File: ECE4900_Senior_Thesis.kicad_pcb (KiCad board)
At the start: 2 copper layers, 9 parts, among them Q1 CSD18540Q5B, Q2 CSD18540Q5B, Q4 CSD18540Q5B, U1 UCC27301ADR, U3 STM32G474CBT6TR, U5 INA240A2DR, U6 INA240A2DR, U7 LM74700QDBVRQ1

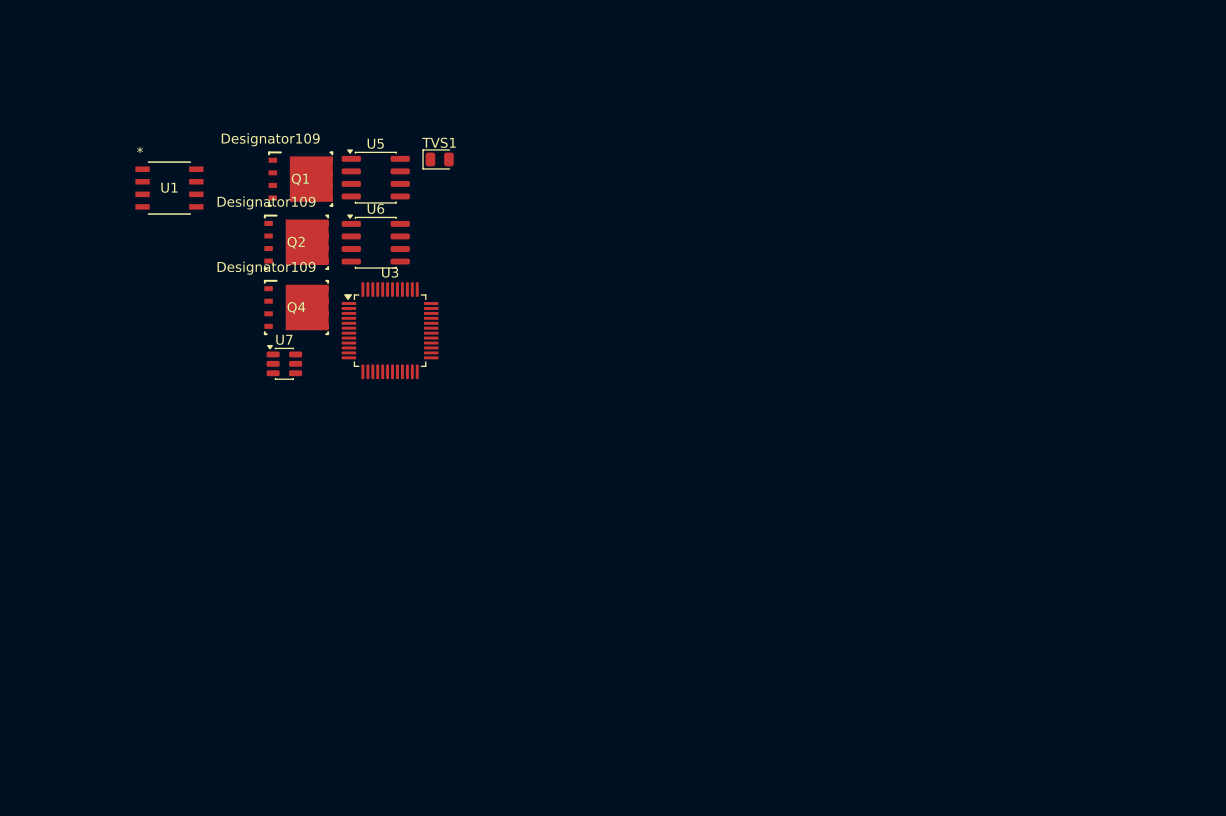
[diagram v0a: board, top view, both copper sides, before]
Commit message: Preliminary Layout Finished
Further pre-fab inspection is neccessary
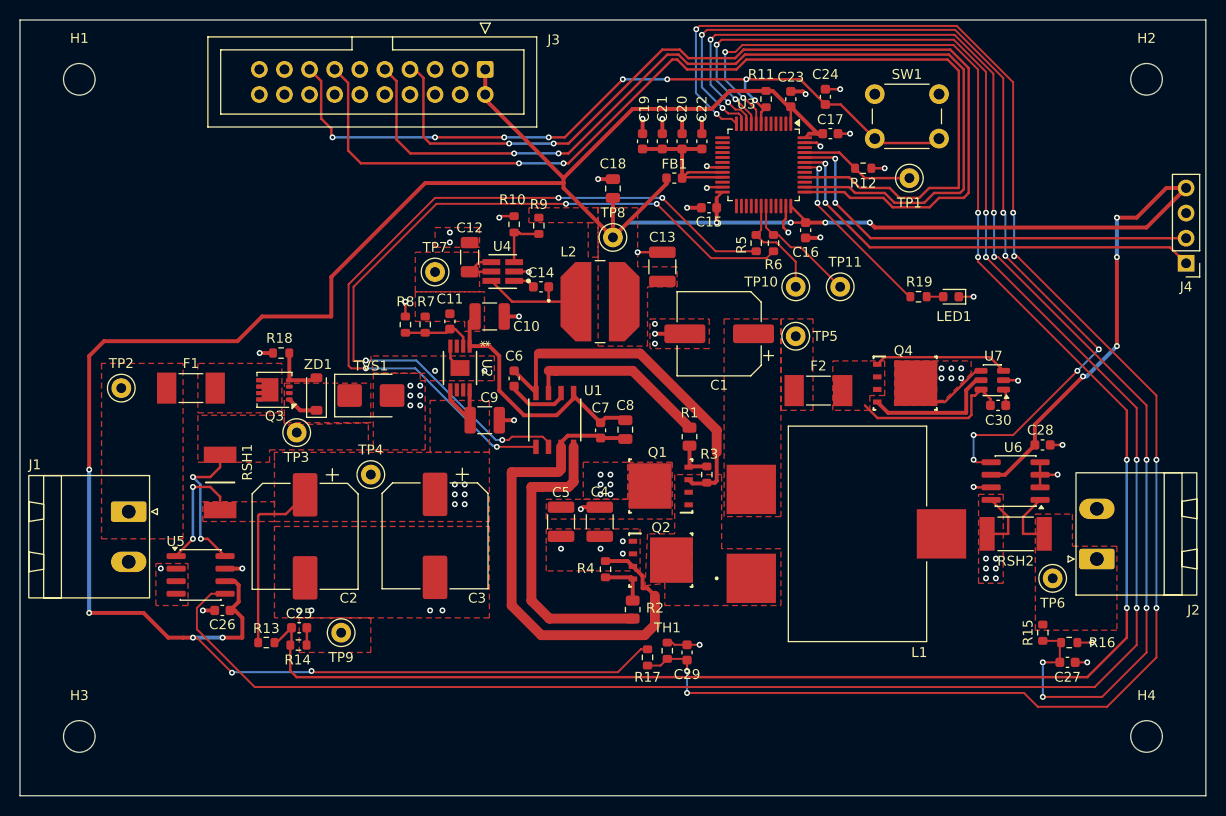
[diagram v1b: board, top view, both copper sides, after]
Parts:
- added C1: 100uF, Capacitor_SMD:CP_Elec_8x6.9, F.Cu at (120.8, 81.8)
- added C10: 10uF, Capacitor_SMD:C_1210_3225Metric, F.Cu at (97.5, 80.0)
- added C11: 10nF, Capacitor_SMD:C_0603_1608Metric, F.Cu at (93.5, 80.5)
- added C12: 4.7uF, Capacitor_SMD:C_1206_3216Metric, F.Cu at (95.5, 74.0)
- added C13: 22uF, Capacitor_SMD:C_1210_3225Metric, F.Cu at (115.0, 75.0)
- added C14: 100nF, Capacitor_SMD:C_0603_1608Metric, F.Cu at (102.7, 77.0)
- added C15: 100nF, Capacitor_SMD:C_0603_1608Metric, F.Cu at (119.7, 69.0)
- added C16: 100nF, Capacitor_SMD:C_0603_1608Metric, F.Cu at (129.5, 71.3)
- added C17: 100nF, Capacitor_SMD:C_0603_1608Metric, F.Cu at (132.0, 61.5)
- added C18: 4.7uF, Capacitor_SMD:C_0805_2012Metric, F.Cu at (110.0, 67.0)
- added C19: 1uF, Capacitor_SMD:C_0603_1608Metric, F.Cu at (113.0, 62.3)
- added C2: 150uF, Capacitor_SMD:CP_Elec_10x12.5, F.Cu at (78.8, 102.2)
- added C20: 100nF, Capacitor_SMD:C_0603_1608Metric, F.Cu at (117.0, 62.3)
- added C21: 1uF, Capacitor_SMD:C_0603_1608Metric, F.Cu at (115.0, 62.3)
- added C22: 100nF, Capacitor_SMD:C_0603_1608Metric, F.Cu at (119.0, 62.3)
- added C23: 100nF, Capacitor_SMD:C_0603_1608Metric, F.Cu at (128.0, 58.0)
- added C24: 100nF, Capacitor_SMD:C_0603_1608Metric, F.Cu at (131.5, 57.8)
- added C25: 10nF, Capacitor_SMD:C_0603_1608Metric, F.Cu at (78.2, 111.5)
- added C26: 100nF, Capacitor_SMD:C_0603_1608Metric, F.Cu at (70.5, 109.8)
- added C27: 10nF, Capacitor_SMD:C_0603_1608Metric, F.Cu at (156.0, 115.0)
- added C28: 100nF, Capacitor_SMD:C_0603_1608Metric, F.Cu at (153.5, 93.0)
- added C29: 10nF, Capacitor_SMD:C_0603_1608Metric, F.Cu at (117.5, 114.0)
- added C3: 150uF, Capacitor_SMD:CP_Elec_10x12.5, F.Cu at (92.0, 102.2)
- added C30: 100nF, Capacitor_SMD:C_0603_1608Metric, F.Cu at (149.0, 89.0)
- added C4: 10uF, Capacitor_SMD:C_1210_3225Metric, F.Cu at (108.7, 100.8)
- added C5: 10uF, Capacitor_SMD:C_1210_3225Metric, F.Cu at (104.8, 100.8)
- added C6: 100nF, Capacitor_SMD:C_0603_1608Metric, F.Cu at (100.0, 86.3)
- added C7: 100nF, Capacitor_SMD:C_0603_1608Metric, F.Cu at (108.8, 91.5)
- added C8: 2.2uF, Capacitor_SMD:C_0805_2012Metric, F.Cu at (111.2, 91.5)
- added C9: 10uF, Capacitor_SMD:C_1210_3225Metric, F.Cu at (97.0, 90.5)
- added F1: 0451007.MRL, Fuse:Fuse_Littelfuse-NANO2-451_453, F.Cu at (67.3, 87.2)
- added F2: 0451010.MRL, Fuse:Fuse_Littelfuse-NANO2-451_453, F.Cu at (130.8, 87.5)
- added FB1: FerriteBead, Inductor_SMD:L_0603_1608Metric, F.Cu at (116.2, 66.0)
- added H1: MountingHole_3.2mm_M3, MountingHole:MountingHole_3.2mm_M3, F.Cu at (56.0, 56.0)
- added H2: MountingHole_3.2mm_M3, MountingHole:MountingHole_3.2mm_M3, F.Cu at (164.0, 56.0)
- added H3: MountingHole_3.2mm_M3, MountingHole:MountingHole_3.2mm_M3, F.Cu at (56.0, 122.5)
- added H4: MountingHole_3.2mm_M3, MountingHole:MountingHole_3.2mm_M3, F.Cu at (164.0, 122.5)
- added J1: 1757242, Connector_Phoenix_MSTB:PhoenixContact_MSTBA_2,5_2-G-5,08_1x02_P5.08mm_Horizontal, F.Cu at (61.0, 99.8)
- added J2: 1757242, Connector_Phoenix_MSTB:PhoenixContact_MSTBA_2,5_2-G-5,08_1x02_P5.08mm_Horizontal, F.Cu at (159.0, 104.5)
- added J3: Conn_02x10_Odd_Even, Connector_IDC:IDC-Header_2x10_P2.54mm_Vertical, F.Cu at (97.1, 55.0)
- added J4: Conn_01x04, Connector_PinHeader_2.54mm:PinHeader_1x04_P2.54mm_Vertical, F.Cu at (168.0, 74.6)
- added L1: 22 uH, FloatingPV:CSCF2014-220MC, F.Cu at (134.8, 102.0)
- added L2: 22uH, FloatingPV:IND_1273AS-H-220M=P3, F.Cu at (108.7, 78.5)
- added LED1: LED, LED_SMD:LED_0603_1608Metric, F.Cu at (144.2, 78.0)
- added Q3: Q_PMOS_GSD, Package_SON:Diodes_PowerDI3333-8, F.Cu at (75.8, 87.4)
- added R1: 10Ω, Resistor_SMD:R_0805_2012Metric, F.Cu at (117.8, 92.2)
- added R10: 22.1kΩ, Resistor_SMD:R_0603_1608Metric, F.Cu at (100.0, 70.7)
- added R11: 10kΩ, Resistor_SMD:R_0603_1608Metric, F.Cu at (125.5, 58.0)
- added R12: 10kΩ, Resistor_SMD:R_0603_1608Metric, F.Cu at (135.3, 65.0)
- added R13: 82kΩ, Resistor_SMD:R_0603_1608Metric, F.Cu at (74.9, 113.0)
- added R14: 10kΩ, Resistor_SMD:R_0603_1608Metric, F.Cu at (78.2, 113.2)
- added R15: 43kΩ, Resistor_SMD:R_0603_1608Metric, F.Cu at (153.5, 112.0)
- added R16: 10kΩ, Resistor_SMD:R_0603_1608Metric, F.Cu at (156.2, 113.0)
- added R17: 10kΩ, Resistor_SMD:R_0603_1608Metric, F.Cu at (113.5, 114.5)
- added R18: 10kΩ, Resistor_SMD:R_0603_1608Metric, F.Cu at (76.4, 83.7)
- added R19: 1kΩ, Resistor_SMD:R_0603_1608Metric, F.Cu at (140.9, 78.0)
- added R2: 10Ω, Resistor_SMD:R_0805_2012Metric, F.Cu at (112.0, 109.7)
- added R3: 10kΩ, Resistor_SMD:R_0603_1608Metric, F.Cu at (119.5, 96.0)
- added R4: 10kΩ, Resistor_SMD:R_0603_1608Metric, F.Cu at (109.2, 105.6)
- added R5: 33Ω, Resistor_SMD:R_0603_1608Metric, F.Cu at (124.5, 72.6)
- added R6: 33Ω, Resistor_SMD:R_0603_1608Metric, F.Cu at (126.2, 72.6)
- added R7: 909kΩ, Resistor_SMD:R_0603_1608Metric, F.Cu at (91.0, 80.8)
- added R8: 100kΩ, Resistor_SMD:R_0603_1608Metric, F.Cu at (89.0, 80.8)
- added R9: 69.8kΩ, Resistor_SMD:R_0603_1608Metric, F.Cu at (102.5, 70.8)
- added RSH1: 10mΩ, FloatingPV:KRL3264E-C-R010-F-T1, F.Cu at (70.2, 96.8)
- added RSH2: 5mΩ, FloatingPV:RESC6432X90N, F.Cu at (150.8, 102.0)
- added SW1: SW_Push, Button_Switch_THT:SW_PUSH_6mm_H4.3mm, F.Cu at (136.5, 57.5)
- added TH1: 10kΩ NTC, Resistor_SMD:R_0603_1608Metric, F.Cu at (115.5, 113.8)
- added TP1: TestPoint, TestPoint:TestPoint_Keystone_5000-5004_Miniature, F.Cu at (140.0, 66.0)
- added TP10: TestPoint, TestPoint:TestPoint_Keystone_5000-5004_Miniature, F.Cu at (128.5, 77.0)
- added TP11: TestPoint, TestPoint:TestPoint_Keystone_5000-5004_Miniature, F.Cu at (133.0, 77.0)
- added TP2: TestPoint, TestPoint:TestPoint_Keystone_5000-5004_Miniature, F.Cu at (60.2, 87.2)
- added TP3: TestPoint, TestPoint:TestPoint_Keystone_5000-5004_Miniature, F.Cu at (78.0, 91.8)
- added TP4: TestPoint, TestPoint:TestPoint_Keystone_5000-5004_Miniature, F.Cu at (85.5, 96.0)
- added TP5: TestPoint, TestPoint:TestPoint_Keystone_5000-5004_Miniature, F.Cu at (128.5, 82.0)
- added TP6: TestPoint, TestPoint:TestPoint_Keystone_5000-5004_Miniature, F.Cu at (154.5, 106.5)
- added TP7: TestPoint, TestPoint:TestPoint_Keystone_5000-5004_Miniature, F.Cu at (92.0, 75.5)
- added TP8: TestPoint, TestPoint:TestPoint_Keystone_5000-5004_Miniature, F.Cu at (110.0, 72.0)
- added TP9: TestPoint, TestPoint:TestPoint_Keystone_5000-5004_Miniature, F.Cu at (82.5, 112.0)
- added U2: TPS7A1601QDGNRQ1, FloatingPV:DGN8_1P92X1P6_TEX, F.Cu at (94.5, 85.2)
- added U4: LMR51610XDBVR, FloatingPV:DBV0006A-IPC_A, F.Cu at (98.8, 75.5)
- added ZD1: BZT52C12-13-F, Diode_SMD:D_SOD-123, F.Cu at (80.0, 87.8)
- TVS1: footprint Diode_SMD:D_0805_2012Metric -> Diode_SMD:D_SMB
- moved U7 71.7 mm to (148.4, 86.5), turned to 180 degrees
- moved U6 69.1 mm to (150.8, 96.7), turned to 180 degrees
- moved Q4 62.1 mm to (139.6, 86.8)
- moved Q2 48.9 mm to (114.8, 104.7)
- moved Q1 47.9 mm to (114.8, 97.2), turned to 180 degrees
- moved U1 45.5 mm to (104.1, 90.5), turned to -90 degrees
- moved U5 43.9 mm to (68.3, 106.2)
- moved U3 41.4 mm to (125.2, 64.7), turned to -90 degrees
- moved TVS1 24.9 mm to (85.5, 88.0)
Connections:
- U1 pad 4: Net-(U1-HS) -> /SW
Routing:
- net /+3V3: track 0.00 -> 337.9 mm, vias 0 -> 14
- net /PV_ISENSE: track 0.00 -> 207.5 mm, vias 0 -> 6
- net /PV_VSENSE: track 0.00 -> 192.6 mm, vias 0 -> 6
- net /TEMP_SENSE: track 0.00 -> 168.6 mm, vias 0 -> 8
- net /BAT_VSENSE: track 0.00 -> 127.6 mm, vias 0 -> 8
- net GND: track 0.00 -> 117.3 mm, vias 0 -> 54
- net /SWO: track 0.00 -> 105.5 mm, vias 0 -> 2
- net Net-(J3-Pin_9): track 0.00 -> 101.1 mm, vias 0 -> 2
- net Net-(J3-Pin_7): track 0.00 -> 99.0 mm, vias 0 -> 2
- net /BAT_ISENSE: track 0.00 -> 96.1 mm, vias 0 -> 8
- net /NRST: track 0.00 -> 80.4 mm, vias 0 -> 8
- net Net-(U1-LI): track 0.00 -> 80.0 mm, vias 0 -> 4
- net Net-(U1-HI): track 0.00 -> 77.7 mm, vias 0 -> 4
- net /UART_TX: track 0.00 -> 45.1 mm, vias 0 -> 2
- net /UART_RX: track 0.00 -> 44.6 mm, vias 0 -> 2
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- added copper zone on F.Cu, net /+12V_AUX
- added copper zone on F.Cu, net /+3V3
- added copper zone on F.Cu, net /BAT_FUSED
- added copper zone on F.Cu, net /BAT_OUT
- added copper zone on F.Cu, net /BAT_PROTECTED
- added copper zone on In2.Cu, net /BAT_PROTECTED
- added copper zone on F.Cu, net /BUCK_OUT
- added copper zone on F.Cu, net /PV_BUS
- added copper zone on In2.Cu, net /PV_BUS
- added copper zone on F.Cu, net /PV_FUSED
- added copper zone on F.Cu, net /PV_IN
- added copper zone on F.Cu, net /PV_PROTECTED
- added copper zone on F.Cu, net /SW
- added copper zone on F.Cu, net GND
- added copper zone on In1.Cu, net GND
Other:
- board outline added: 120 x 78.5 mm
- copper layers 2 -> 4
